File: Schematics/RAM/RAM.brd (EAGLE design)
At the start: 94.2 x 106.3 mm, 35 parts

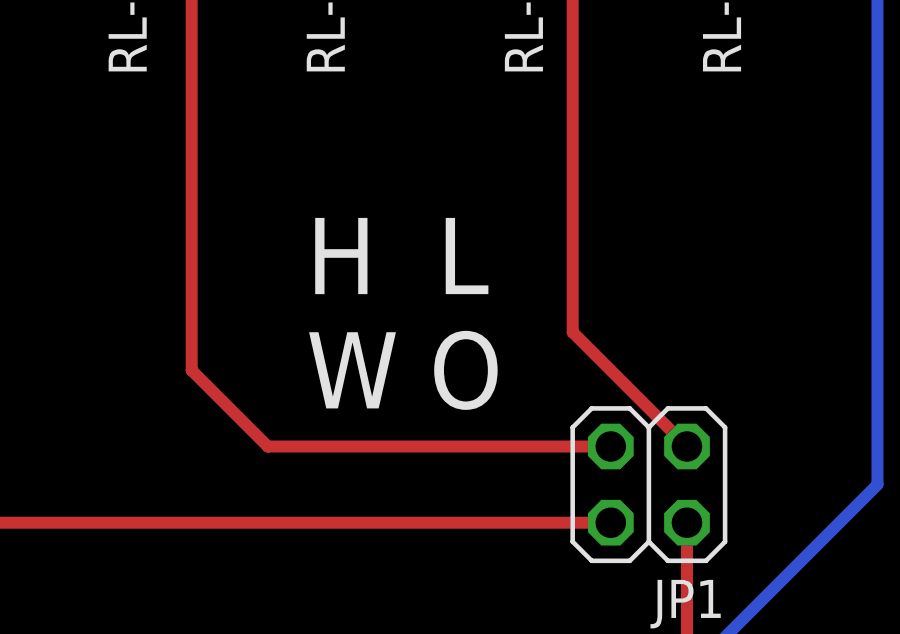
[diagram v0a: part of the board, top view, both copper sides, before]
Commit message: Register, PC, RAM will be solid board not modules, brd is pretty simple.
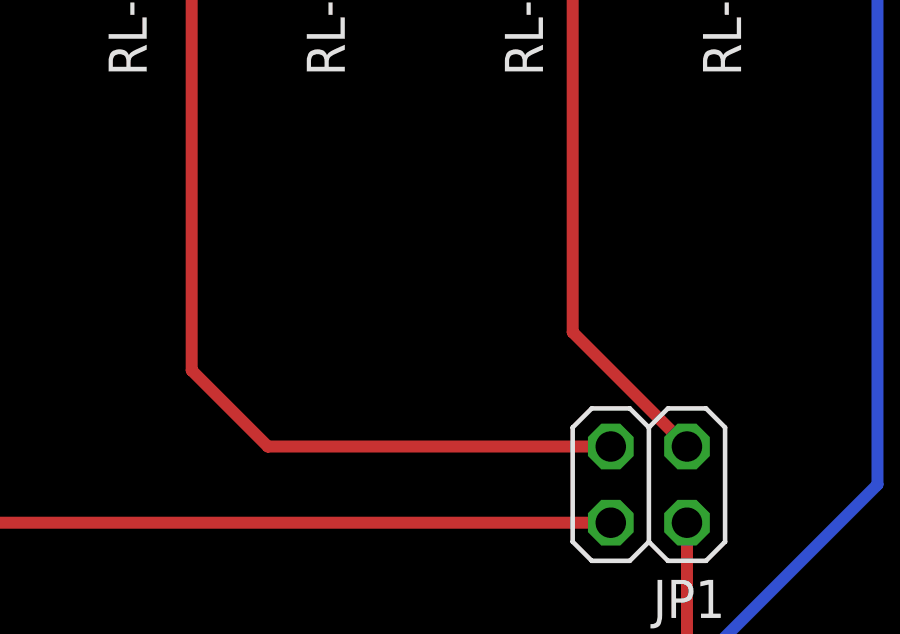
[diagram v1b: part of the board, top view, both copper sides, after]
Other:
- board text removed: "H L W O"
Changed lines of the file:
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@@
 <wire x1="0" y1="106.35" x2="0" y2="0" width="0" layer="20"/>
 <text x="8.89" y="91.44" size="6.4516" layer="21">RAM</text>
-<text x="71.12" y="38.1" size="2.54" layer="21">H  L
-W O</text>
 </plain>
 <attributes>
@@
 </drawing>
 <compatibility>
-<note version="6.3" minversion="6.2.2" severity="warning">
-Since Version 6.2.2 text objects can contain more than one line,
-which will not be processed correctly with this version.
-</note>
 <note version="8.2" severity="warning">
 Since Version 8.2, EAGLE supports online libraries. The ids
